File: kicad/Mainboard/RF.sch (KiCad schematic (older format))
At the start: 58 parts, among them J7 Antenna, T1 AFT05MS004NT1, U5 HMC546MS8GETR, U6 SI4463-C2A-GM, X1 ILSI 32MHz TCXO

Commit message: Updated WIP schematics
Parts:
- removed C23: 1u/TA, symbol Mainboard-rescue:C_Small-device
- removed R7: 1k, symbol Mainboard-rescue:R_Small-device
- removed R8: 8k2, symbol Mainboard-rescue:R_Small-device
- removed RV1: 10k, symbol Mainboard-rescue:R_POT_TRIM-device
- added C?: 100n, symbol Device:C_Small
- added C?: 10n, symbol Device:C_Small
- added C?: 1n, symbol Device:C_Small
- added R?: TBD, symbol Device:R_Small
- added U? (x3): LM2904, symbol Amplifier_Operational:LM2904
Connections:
- net labels added: DAC_PA
- net labels removed: PDET
- wire segments 168 -> 177
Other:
- moved on the sheet: C21, C22, C24, C25, C26, C27, C28, C29, C30, C31, C32, C33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

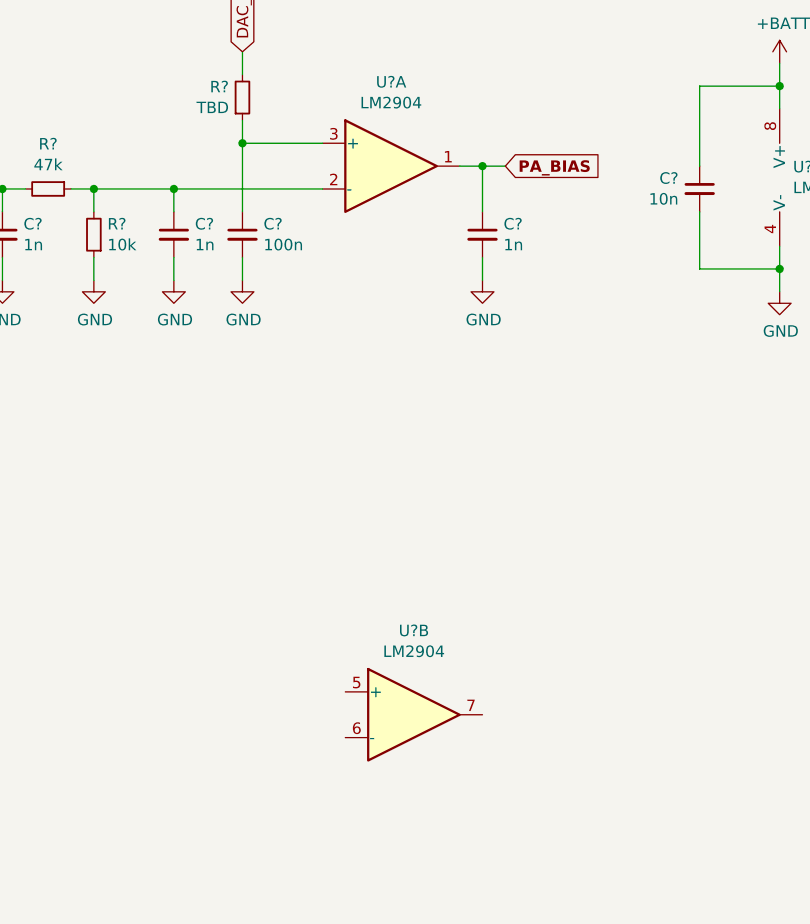
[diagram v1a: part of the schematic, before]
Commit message: Add files via upload
* replaced Q7 with BSS138
* new HMI connector (for keypad and display)
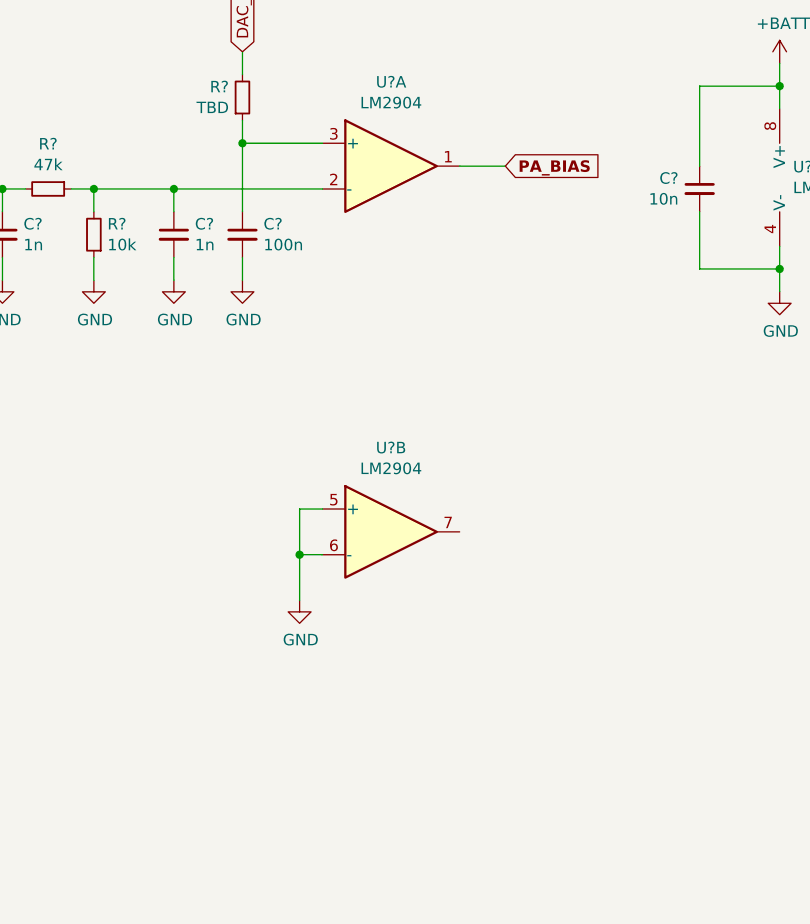
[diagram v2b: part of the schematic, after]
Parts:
- removed C?: 1n, symbol Device:C_Small
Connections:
- wire segments 177 -> 178
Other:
- moved on the sheet: U?B
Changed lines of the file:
@@
 EESchema Schematic File Version 4
+LIBS:Mainboard-cache
 EELAYER 30 0
 EELAYER END
@@
 L Amplifier_Operational:LM2904 U?
 U 2 1 5E1864A9
-P 11650 6700
-F 0 "U?" H 11650 7067 50  0000 C CNN
-F 1 "LM2904" H 11650 6976 50  0000 C CNN
-F 2 "" H 11650 6700 50  0001 C CNN
-F 3 "http://www.ti.com/lit/ds/symlink/lm358.pdf" H 11650 6700 50  0001 C CNN
-	2    11650 6700
+P 11550 5900
+F 0 "U?" H 11550 6267 50  0000 C CNN
+F 1 "LM2904" H 11550 6176 50  0000 C CNN
+F 2 "" H 11550 5900 50  0001 C CNN
+F 3 "http://www.ti.com/lit/ds/symlink/lm358.pdf" H 11550 5900 50  0001 C CNN
+	2    11550 5900
 	1    0    0    -1
 $EndComp
@@
 Connection ~ 13250 4750
 Wire Wire Line
-	11850 4300 11950 4300
-$Comp
-L Device:C_Small C?
-U 1 1 5E1E7F2E
-P 11950 4600
-F 0 "C?" H 12042 4646 50  0000 L CNN
-F 1 "1n" H 12042 4555 50  0000 L CNN
-F 2 "" H 11950 4600 50  0001 C CNN
-F 3 "~" H 11950 4600 50  0001 C CNN
-	1    11950 4600
-	1    0    0    -1
-$EndComp
-Wire Wire Line
-	11950 4300 11950 4500
-$Comp
-L power:GND #PWR?
-U 1 1 5E1F0CAF
-P 11950 4800
-F 0 "#PWR?" H 11950 4550 50  0001 C CNN
-F 1 "GND" H 11955 4627 50  0000 C CNN
-F 2 "" H 11950 4800 50  0001 C CNN
-F 3 "" H 11950 4800 50  0001 C CNN
-	1    11950 4800
-	1    0    0    -1
-$EndComp
-Wire Wire Line
-	11950 4700 11950 4800
-Wire Wire Line
-	11950 4300 12050 4300
-Connection ~ 11950 4300
-Wire Wire Line
 	3550 2150 3550 2250
 Connection ~ 3550 2250
+$Comp
+L power:GND #PWR?
+U 1 1 5E212E0D
+P 11150 6200
+F 0 "#PWR?" H 11150 5950 50  0001 C CNN
+F 1 "GND" H 11155 6027 50  0000 C CNN
+F 2 "" H 11150 6200 50  0001 C CNN
+F 3 "" H 11150 6200 50  0001 C CNN
+	1    11150 6200
+	1    0    0    -1
+$EndComp
+Wire Wire Line
+	11250 5800 11150 5800
+Wire Wire Line
+	11150 5800 11150 6000
+Wire Wire Line
+	11250 6000 11150 6000
+Connection ~ 11150 6000
+Wire Wire Line
+	11150 6000 11150 6200
+Wire Wire Line
+	11850 4300 12050 4300
 $EndSCHEMATC

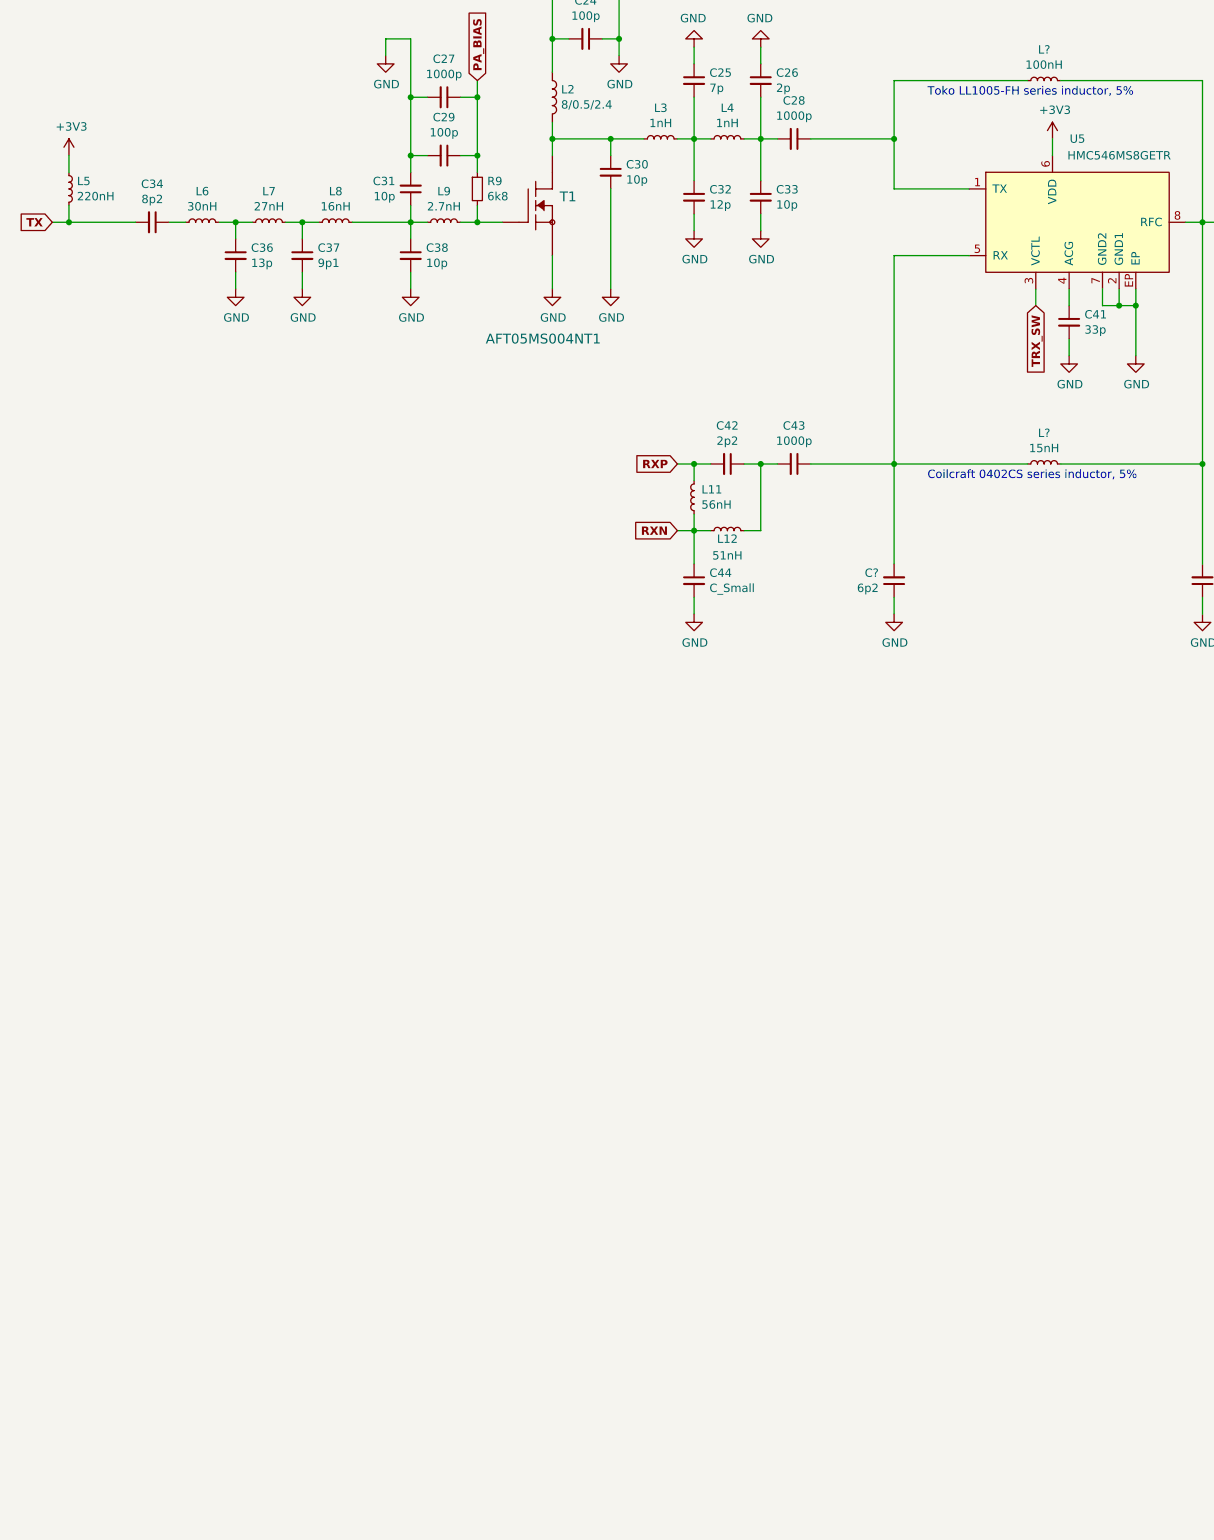
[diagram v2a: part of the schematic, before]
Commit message: Added ADF7021
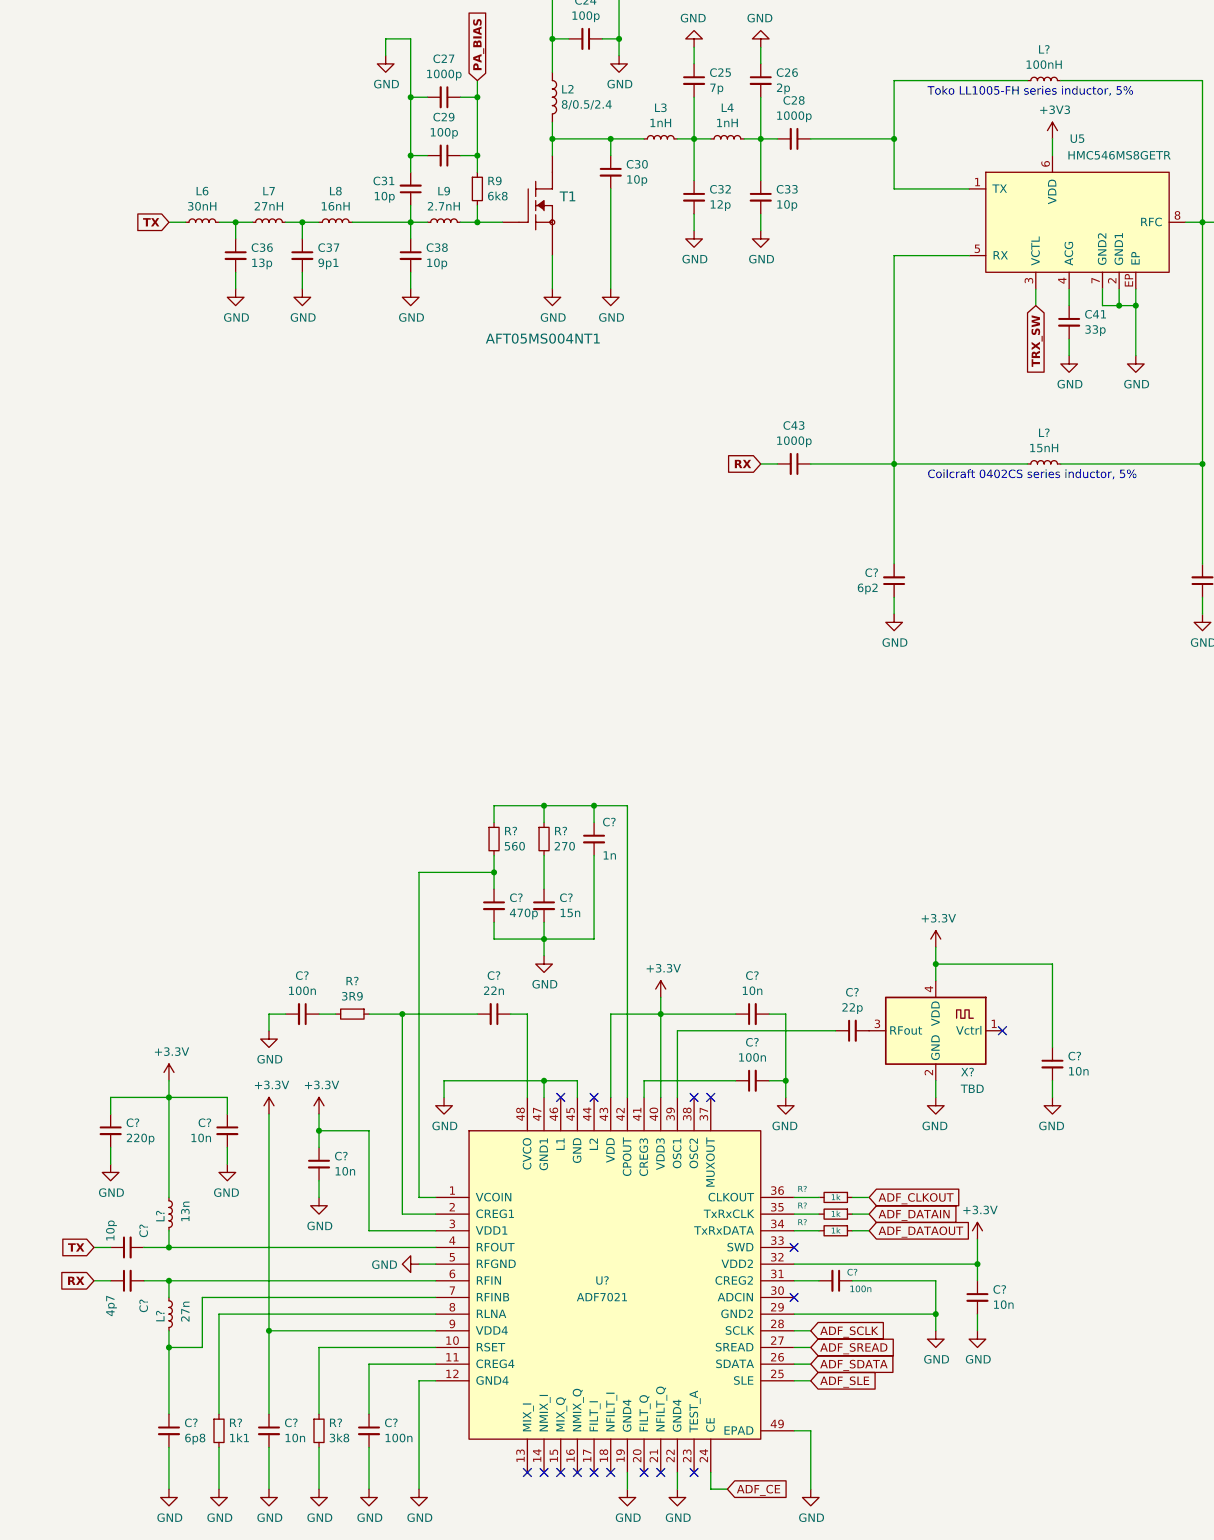
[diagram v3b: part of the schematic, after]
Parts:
- removed C34: 8p2, symbol Mainboard-rescue:C_Small-device
- removed C42: 2p2, symbol Mainboard-rescue:C_Small-device
- removed C44: C_Small, symbol Mainboard-rescue:C_Small-device
- removed L11: 56nH, symbol Mainboard-rescue:L_Small-device
- removed L12: 51nH, symbol Mainboard-rescue:L_Small-device
- removed L5: 220nH, symbol Mainboard-rescue:L_Small-device
- added C? (x4): 100n, symbol Device:C_Small
- added C? (x6): 10n, symbol Device:C_Small
- added C?: 6p8, symbol Device:C_Small
- added C?: 4p7, symbol Device:C_Small
- added C?: 10p, symbol Device:C_Small
- added C?: 220p, symbol Device:C_Small
- added C?: 22n, symbol Device:C_Small
- added C?: 1n, symbol Device:C_Small
- added C?: 470p, symbol Device:C_Small
- added C?: 15n, symbol Device:C_Small
- added C?: 22p, symbol Device:C_Small
- added L?: 27n, symbol Device:L_Small
- added L?: 13n, symbol Device:L_Small
- added R? (x3): 1k, symbol Device:R_Small
- added R?: 3k8, symbol Device:R_Small
- added R?: 1k1, symbol Device:R_Small
- added R?: 3R9, symbol Device:R_Small
- added R?: 560, symbol Device:R_Small
- added R?: 270, symbol Device:R_Small
- added U?: ADF7021, symbol adf7021:ADF7021
- added X?: TBD, Oscillator:Oscillator_SMD_Abracon_ABLNO, symbol Oscillator:ABLNO
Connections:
- net labels added: +3.3V, ADF_CE, ADF_CLKOUT, ADF_DATAIN, ADF_DATAOUT, ADF_SCLK, ADF_SDATA, ADF_SLE, ADF_SREAD, RX
- wire segments 178 -> 284
- no-connect marks 7 -> 23

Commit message: Added BGA6589 gain stage
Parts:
- removed C36: 13p, symbol Mainboard-rescue:C_Small-device
- removed C37: 9p1, symbol Mainboard-rescue:C_Small-device
- removed C45: 10n, symbol Mainboard-rescue:C_Small-device
- removed L6: 30nH, symbol Mainboard-rescue:L_Small-device
- removed L7: 27nH, symbol Mainboard-rescue:L_Small-device
- removed L8: 16nH, symbol Mainboard-rescue:L_Small-device
- removed U6: SI4463-C2A-GM, symbol TR-9:SI4463-C2A-GM
- removed X1: ILSI 32MHz TCXO, symbol TR-9:ASE
- added C?: 6p8, symbol Device:C_Small
- added C? (x2): 220p, symbol Device:C_Small
- added C?: 100p, symbol Device:C_Small
- added C?: 1n, symbol Device:C_Small
- added C?: 1u, symbol Device:CP_Small
- added L?: 20n, symbol Device:L_Small
- added L?: 22n, symbol Device:L_Small
- added L?: 68nH, symbol Device:L_Small
- added Q?: BGA6589, symbol TR-9:BGA6589
- added R?: 51, symbol Device:R_Small
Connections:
- net labels removed: RXN, RXP, SPI2_CS, SPI2_MISO, SPI2_MOSI, SPI2_SCK, TRX_NIRQ, TRX_SDN
- wire segments 284 -> 280
- no-connect marks 23 -> 16
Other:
- note added: "0.5W"
- note added: "TODO: RX filtering"
- moved on the sheet: C21, C22, C24, C25, C26, C27, C28, C29, C30, C31, C32, C33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

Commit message: Add files via upload
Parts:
- removed C27: 1000p, symbol Mainboard-rescue:C_Small-device
- removed C29: 100p, symbol Mainboard-rescue:C_Small-device
- removed R? (x3): 1k, symbol Device:R_Small
- added C?: 100n, symbol Device:C_Small
- added R? (x3): 1k, symbol Device:R_Small
- added R?: 100, symbol Device:R_Small
- added R?: 100k, symbol Device:R_Small
- added TP? (x3): TestPoint_Probe, symbol Connector:TestPoint_Probe
- L?: value 13n -> 15n
- R?: value 3k8 -> 3k6
- X?: value TBD -> 14.7456MHz
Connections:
- net ADF_CLKOUT: now also R?.1
- net ADF_DATAIN: now also R?.1
- net ADF_DATAOUT: now also R?.1
- net at C?.1, R?.2: now also R?.1, TP?.1; no longer U?.1 (VCOIN)
- net ADF_SWD: now reaches U?.33 (SWD)
- net at U?.34 (TxRxDATA): now also R?.2
- net at U?.35 (TxRxCLK): now also R?.2
- net at U?.36 (CLKOUT): now also R?.2
- net at C?.1, R?.1, R?.1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: now also TP?.1
- new net: R?.1, R?.2, TP?.1, U?.1 (VCOIN)
- new net: C?.1, R?.2
- new net FM_MOD: C?.2
- no-connect marks 16 -> 15
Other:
- note added: "Voltage at this point should be 0.2-2V"
- moved on the sheet: C?, L?, R?, U?, X?

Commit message: Add files via upload
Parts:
- added C?: 2n2, symbol Device:C_Small
- added R?: 22k, symbol Device:R_Small
- added R?: 47k, symbol Device:R_Small
- R?: value 100k -> 47k
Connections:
- net FM_MOD: now also R?.1, R?.2; no longer C?.2
- net GND: now also C?.1, R?.1
- net DAC_PA renamed PA_RAMP
- new net: C?.2, C?.2, R?.2
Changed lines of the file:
@@
 Wire Wire Line
 	13250 3900 13250 3800
-Text GLabel 13250 3800 1    50   Input ~ 0
-DAC_PA
+Text GLabel 13250 3800 1    50   Input ~ 10
+PA_RAMP
 $Comp
 L Device:C_Small C?
@@
 	5050 6700 5050 6200
 Connection ~ 4750 6700
-$Comp
-L power:GND #PWR?
-U 1 1 5E8261D5
-P 4750 6800
-F 0 "#PWR?" H 4750 6550 50  0001 C CNN
-F 1 "GND" H 4755 6627 50  0000 C CNN
-F 2 "" H 4750 6800 50  0001 C CNN
-F 3 "" H 4750 6800 50  0001 C CNN
-	1    4750 6800
-	1    0    0    -1
-$EndComp
 Wire Wire Line
 	4750 6700 4750 6800
@@
 P 3750 6300
 F 0 "R?" V 3554 6300 50  0000 C CNN
-F 1 "100k" V 3645 6300 50  0000 C CNN
+F 1 "47k" V 3645 6300 50  0000 C CNN
 F 2 "" H 3750 6300 50  0001 C CNN
 F 3 "~" H 3750 6300 50  0001 C CNN
@@
 Wire Wire Line
 	3650 6300 3550 6300
-Wire Wire Line
-	3350 6300 3200 6300
-Text GLabel 3200 6300 0    50   Input ~ 0
+Text GLabel 2550 6300 0    50   Input ~ 0
 FM_MOD
 Text Notes 4350 5700 2    50   ~ 0
@@
 Wire Wire Line
 	5250 6300 5250 5900
+$Comp
+L Device:R_Small R?
+U 1 1 5E462A64
+P 2650 6450
+F 0 "R?" V 2454 6450 50  0000 C CNN
+F 1 "22k" V 2545 6450 50  0000 C CNN
+F 2 "" H 2650 6450 50  0001 C CNN
+F 3 "~" H 2650 6450 50  0001 C CNN
+	1    2650 6450
+	-1   0    0    1
+$EndComp
+$Comp
+L power:GND #PWR?
+U 1 1 5E8261D5
+P 4750 6800
+F 0 "#PWR?" H 4750 6550 50  0001 C CNN
+F 1 "GND" H 4755 6627 50  0000 C CNN
+F 2 "" H 4750 6800 50  0001 C CNN
+F 3 "" H 4750 6800 50  0001 C CNN
+	1    4750 6800
+	1    0    0    -1
+$EndComp
+$Comp
+L power:GND #PWR?
+U 1 1 5E47AF06
+P 2650 6650
+F 0 "#PWR?" H 2650 6400 50  0001 C CNN
+F 1 "GND" H 2655 6477 50  0000 C CNN
+F 2 "" H 2650 6650 50  0001 C CNN
+F 3 "" H 2650 6650 50  0001 C CNN
+	1    2650 6650
+	1    0    0    -1
+$EndComp
+Wire Wire Line
+	2550 6300 2650 6300
+Wire Wire Line
+	2650 6300 2650 6350
+Wire Wire Line
+	2650 6550 2650 6650
+$Comp
+L Device:R_Small R?
+U 1 1 5E4AF468
+P 2950 6300
+F 0 "R?" V 2754 6300 50  0000 C CNN
+F 1 "47k" V 2845 6300 50  0000 C CNN
+F 2 "" H 2950 6300 50  0001 C CNN
+F 3 "~" H 2950 6300 50  0001 C CNN
+	1    2950 6300
+	0    -1   -1   0
+$EndComp
+$Comp
+L Device:C_Small C?
+U 1 1 5E4AF96C
+P 3150 6450
+F 0 "C?" V 2921 6450 50  0000 C CNN
+F 1 "2n2" V 3012 6450 50  0000 C CNN
+F 2 "" H 3150 6450 50  0001 C CNN
+F 3 "~" H 3150 6450 50  0001 C CNN
+	1    3150 6450
+	-1   0    0    1
+$EndComp
+$Comp
+L power:GND #PWR?
+U 1 1 5E4C885A
+P 3150 6650
+F 0 "#PWR?" H 3150 6400 50  0001 C CNN
+F 1 "GND" H 3155 6477 50  0000 C CNN
+F 2 "" H 3150 6650 50  0001 C CNN
+F 3 "" H 3150 6650 50  0001 C CNN
+	1    3150 6650
+	1    0    0    -1
+$EndComp
+Wire Wire Line
+	3150 6550 3150 6650
+Wire Wire Line
+	3150 6350 3150 6300
+Connection ~ 3150 6300
+Wire Wire Line
+	3150 6300 3350 6300
+Wire Wire Line
+	2850 6300 2650 6300
+Connection ~ 2650 6300
+Wire Wire Line
+	3050 6300 3150 6300
 $EndSCHEMATC
